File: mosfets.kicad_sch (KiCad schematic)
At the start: 38 parts, among them Q1 IXFK300N20X3, Q2 IXFK300N20X3, Q3 IXFK300N20X3, Q4 IXFK300N20X3, Q5 IXFK300N20X3, Q6 IXFK300N20X3, U1 ACS781xLRTR-150B, U2 ACS781xLRTR-150B, U3 ACS781xLRTR-150B

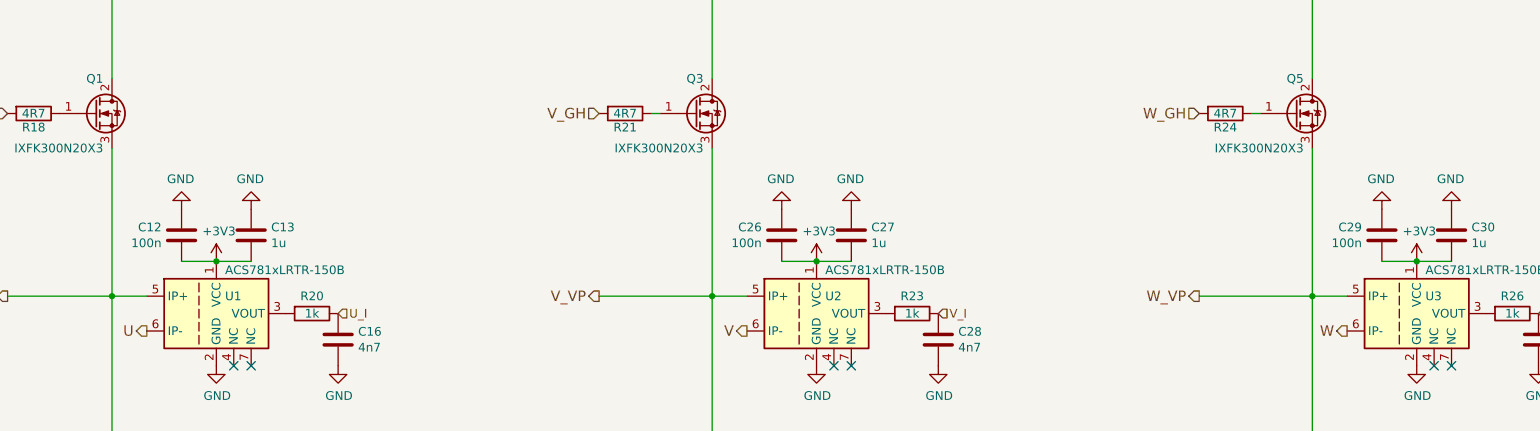
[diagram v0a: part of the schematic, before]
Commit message: - peeled back the filler planes around HV logic - improved insulation on HV logic
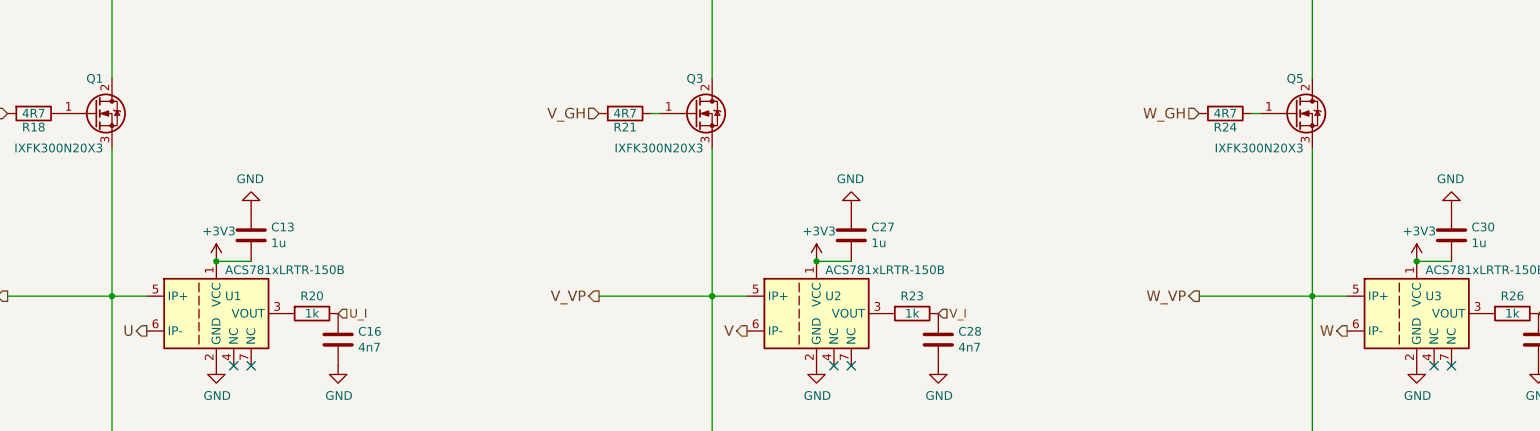
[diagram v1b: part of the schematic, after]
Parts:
- removed C12, C26, C29: 100n, Capacitor_SMD:C_0805_2012Metric, symbol Device:C
- C20, C21, C22, C23, C24, C25: footprint Capacitor_SMD:C_2220_5650Metric -> Capacitor_SMD:C_2220_5750Metric
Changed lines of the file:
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@@
-    (stroke (width 0) (type default))
-  )
-  (wire (pts (xy 149.86 87.63) (xy 154.94 87.63))
     (stroke (width 0) (type default))
   )
@@
     (stroke (width 0) (type default))
   )
-  (wire (pts (xy 62.23 87.63) (xy 67.31 87.63))
-    (stroke (width 0) (type default))
-  )
   (wire (pts (xy 242.57 87.63) (xy 247.65 87.63))
     (stroke (width 0) (type default))
@@
   )
   (wire (pts (xy 121.92 177.8) (xy 128.27 177.8))
-    (stroke (width 0) (type default))
-  )
-  (wire (pts (xy 237.49 87.63) (xy 242.57 87.63))
     (stroke (width 0) (type default))
   )
@@
       (effects (font (size 1.27 1.27)) (justify left))
     )
-    (property "Footprint" "Capacitor_SMD:C_2220_5650Metric" (at 114.6048 185.42 0)
+    (property "Footprint" "Capacitor_SMD:C_2220_5750Metric" (at 114.6048 185.42 0)
       (effects (font (size 1.27 1.27)) hide)
     )
@@
       (effects (font (size 1.27 1.27)) (justify left))
     )
-    (property "Footprint" "Capacitor_SMD:C_2220_5650Metric" (at 122.8852 185.42 0)
+    (property "Footprint" "Capacitor_SMD:C_2220_5750Metric" (at 122.8852 185.42 0)
       (effects (font (size 1.27 1.27)) hide)
     )
@@
       (effects (font (size 1.27 1.27)) (justify left))
     )
-    (property "Footprint" "Capacitor_SMD:C_2220_5650Metric" (at 127.3048 185.42 0)
+    (property "Footprint" "Capacitor_SMD:C_2220_5750Metric" (at 127.3048 185.42 0)
       (effects (font (size 1.27 1.27)) hide)
     )
@@
       (effects (font (size 1.27 1.27)) (justify left))
     )
-    (property "Footprint" "Capacitor_SMD:C_2220_5650Metric" (at 135.5852 185.42 0)
+    (property "Footprint" "Capacitor_SMD:C_2220_5750Metric" (at 135.5852 185.42 0)
       (effects (font (size 1.27 1.27)) hide)
     )
@@
       (effects (font (size 1.27 1.27)) (justify left))
     )
-    (property "Footprint" "Capacitor_SMD:C_2220_5650Metric" (at 140.0048 185.42 0)
+    (property "Footprint" "Capacitor_SMD:C_2220_5750Metric" (at 140.0048 185.42 0)
       (effects (font (size 1.27 1.27)) hide)
     )
@@
       (effects (font (size 1.27 1.27)) (justify left))
     )
-    (property "Footprint" "Capacitor_SMD:C_2220_5650Metric" (at 148.2852 185.42 0)
+    (property "Footprint" "Capacitor_SMD:C_2220_5750Metric" (at 148.2852 185.42 0)
       (effects (font (size 1.27 1.27)) hide)
     )
@@
     )
   )
-  (symbol (lib_id "Device:C") (at 62.23 83.82 0) (mirror x) (unit 1)
-    (in_bom yes) (on_board yes) (dnp no)
-    (property "Reference" "C12" (at 59.309 82.6516 0)
-      (effects (font (size 1.27 1.27)) (justify right))
-    )
-    (property "Value" "100n" (at 59.309 84.963 0)
-      (effects (font (size 1.27 1.27)) (justify right))
-    )
-    (property "Footprint" "Capacitor_SMD:C_0805_2012Metric" (at 63.1952 80.01 0)
-      (effects (font (size 1.27 1.27)) hide)
-    )
-    (property "Datasheet" "~" (at 62.23 83.82 0)
-      (effects (font (size 1.27 1.27)) hide)
-    )
-    (pin "1")
-    (pin "2")
-    (instances
-      (project "HSWR"
-        (path "/51094070-255e-40e7-bed5-d199e288e5dd/00000000-0000-0000-0000-00005895e67a"
-          (reference "C12") (unit 1)
-        )
-      )
-    )
-  )
   (symbol (lib_id "Device:C") (at 72.39 83.82 0) (unit 1)
     (in_bom yes) (on_board yes) (dnp no)
@@
     )
   )
-  (symbol (lib_id "power:GND") (at 62.23 80.01 180) (unit 1)
-    (in_bom yes) (on_board yes) (dnp no)
-    (property "Reference" "#PWR043" (at 62.23 73.66 0)
-      (effects (font (size 1.27 1.27)) hide)
-    )
-    (property "Value" "GND" (at 62.103 75.6158 0)
-      (effects (font (size 1.27 1.27)))
-    )
-    (property "Footprint" "" (at 62.23 80.01 0)
-      (effects (font (size 1.27 1.27)) hide)
-    )
-    (property "Datasheet" "" (at 62.23 80.01 0)
-      (effects (font (size 1.27 1.27)) hide)
-    )
-    (pin "1")
-    (instances
-      (project "HSWR"
-        (path "/51094070-255e-40e7-bed5-d199e288e5dd/00000000-0000-0000-0000-00005895e67a"
-          (reference "#PWR043") (unit 1)
-        )
-      )
-    )
-  )
   (symbol (lib_id "power:GND") (at 72.39 80.01 180) (unit 1)
     (in_bom yes) (on_board yes) (dnp no)
@@
     )
   )
-  (symbol (lib_id "Device:C") (at 149.86 83.82 0) (mirror x) (unit 1)
-    (in_bom yes) (on_board yes) (dnp no)
-    (property "Reference" "C26" (at 146.939 82.6516 0)
-      (effects (font (size 1.27 1.27)) (justify right))
-    )
-    (property "Value" "100n" (at 146.939 84.963 0)
-      (effects (font (size 1.27 1.27)) (justify right))
-    )
-    (property "Footprint" "Capacitor_SMD:C_0805_2012Metric" (at 150.8252 80.01 0)
-      (effects (font (size 1.27 1.27)) hide)
-    )
-    (property "Datasheet" "~" (at 149.86 83.82 0)
-      (effects (font (size 1.27 1.27)) hide)
-    )
-    (pin "1")
-    (pin "2")
-    (instances
-      (project "HSWR"
-        (path "/51094070-255e-40e7-bed5-d199e288e5dd/00000000-0000-0000-0000-00005895e67a"
-          (reference "C26") (unit 1)
-        )
-      )
-    )
-  )
   (symbol (lib_id "Device:C") (at 160.02 83.82 0) (unit 1)
     (in_bom yes) (on_board yes) (dnp no)
@@
     )
   )
-  (symbol (lib_id "power:GND") (at 149.86 80.01 180) (unit 1)
-    (in_bom yes) (on_board yes) (dnp no)
-    (property "Reference" "#PWR052" (at 149.86 73.66 0)
-      (effects (font (size 1.27 1.27)) hide)
-    )
-    (property "Value" "GND" (at 149.733 75.6158 0)
-      (effects (font (size 1.27 1.27)))
-    )
-    (property "Footprint" "" (at 149.86 80.01 0)
-      (effects (font (size 1.27 1.27)) hide)
-    )
-    (property "Datasheet" "" (at 149.86 80.01 0)
-      (effects (font (size 1.27 1.27)) hide)
-    )
-    (pin "1")
-    (instances
-      (project "HSWR"
-        (path "/51094070-255e-40e7-bed5-d199e288e5dd/00000000-0000-0000-0000-00005895e67a"
-          (reference "#PWR052") (unit 1)
-        )
-      )
-    )
-  )
   (symbol (lib_id "power:GND") (at 160.02 80.01 180) (unit 1)
     (in_bom yes) (on_board yes) (dnp no)
@@
     )
   )
-  (symbol (lib_id "Device:C") (at 237.49 83.82 0) (mirror x) (unit 1)
-    (in_bom yes) (on_board yes) (dnp no)
-    (property "Reference" "C29" (at 234.569 82.6516 0)
-      (effects (font (size 1.27 1.27)) (justify right))
-    )
-    (property "Value" "100n" (at 234.569 84.963 0)
-      (effects (font (size 1.27 1.27)) (justify right))
-    )
-    (property "Footprint" "Capacitor_SMD:C_0805_2012Metric" (at 238.4552 80.01 0)
-      (effects (font (size 1.27 1.27)) hide)
-    )
-    (property "Datasheet" "~" (at 237.49 83.82 0)
-      (effects (font (size 1.27 1.27)) hide)
-    )
-    (pin "1")
-    (pin "2")
-    (instances
-      (project "HSWR"
-        (path "/51094070-255e-40e7-bed5-d199e288e5dd/00000000-0000-0000-0000-00005895e67a"
-          (reference "C29") (unit 1)
-        )
-      )
-    )
-  )
   (symbol (lib_id "Device:C") (at 247.65 83.82 0) (unit 1)
     (in_bom yes) (on_board yes) (dnp no)
@@
         )
       )
-    )
-  )
-  (symbol (lib_id "power:GND") (at 237.49 80.01 180) (unit 1)
-    (in_bom yes) (on_board yes) (dnp no)
-    (property "Reference" "#PWR059" (at 237.49 73.66 0)
-      (effects (font (size 1.27 1.27)) hide)
-    )
-    (property "Value" "GND" (at 237.363 75.6158 0)
-      (effects (font (size 1.27 1.27)))
-    )
-    (property "Footprint" "" (at 237.49 80.01 0)
-      (effects (font (size 1.27 1.27)) hide)
-    )
-    (property "Datasheet" "" (at 237.49 80.01 0)
-      (effects (font (size 1.27 1.27)) hide)
-    )
-    (pin "1")
-    (instances
-      (project "HSWR"
-        (path "/51094070-255e-40e7-bed5-d199e288e5dd/00000000-0000-0000-0000-00005895e67a"
-          (reference "#PWR059") (unit 1)
-        )
-      )
